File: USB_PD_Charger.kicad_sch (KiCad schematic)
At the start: 50 parts, among them J9 Conn_01x05, Q1 AOSP21321, Q2 BSH105,215, Q3 BSH105,215, Q4 BSH105,215, U1 LM3489QMM/NOPB, U2 TPS65987DDHRSHR, U3 MX25L8006EM1I-12G

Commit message: Updated schematics
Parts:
- added R30, R31: 1k, Resistor_SMD:R_0402_1005Metric, symbol Device:R_Small
- C18: LCSC C541323 -> C1603; Part_Number CC0201JRX7R8BB221 -> CL10B221KB8NNNC
- C20, C5: LCSC C105883 -> C307331; Part_Number CC0402KRX7R8BB104 -> CL05B104KB54PNC
- C21: LCSC C59782 -> C15849; Part_Number CL10B105KO8NNNC -> CL10A105KB8NNNC
- C24, C25: footprint Capacitor_SMD:C_0603_1608Metric -> Capacitor_SMD:C_0402_1005Metric; LCSC C19702 -> C15525; Part_Number CL10A106KP8NNNC -> CL05A106MQ5NUNC
- C6, C9: LCSC C106205 -> C1523; Part_Number CC0402KRX7R9BB102 -> 0402B102K500NT
- C7: value 0.1uF -> 0.1µF; LCSC C187828 -> C307331; Part_Number GMK105BJ104KV-F -> CL05B104KB54PNC
- C8: LCSC C281751 -> C1546; Part_Number CC0402KRX7R9BB101 -> 0402CG101J500NT
- R1: LCSC C107699 -> C17514; Part_Number RC0805JR-071ML -> 0805W8F1004T5E
- R10: footprint Resistor_SMD:R_0402_1005Metric -> Resistor_SMD:R_0805_2012Metric_Pad1.20x1.40mm_HandSolder; LCSC C321660 -> C17858; Part_Number RC-02W9531FT -> 0805W8F9531T5E
- R11, R12, R13, R5: footprint Resistor_SMD:R_0402_1005Metric -> Resistor_SMD:R_0603_1608Metric; LCSC C284273 -> C25803; Part_Number ARG02FTC1003 -> 0603WAF1003T5E
- R14: footprint Resistor_SMD:R_0402_1005Metric -> Resistor_SMD:R_0805_2012Metric_Pad1.20x1.40mm_HandSolder; LCSC C310249 -> C37551; Part_Number RC-02W8871FT -> 0805W8F8871T5E
- R15: footprint Resistor_SMD:R_0402_1005Metric -> Resistor_SMD:R_0805_2012Metric_Pad1.20x1.40mm_HandSolder; LCSC C166578 -> C17611; Part_Number RTT023651FTH -> 0805W8F3651T5E
- R16: footprint Resistor_SMD:R_0402_1005Metric -> Resistor_SMD:R_0805_2012Metric_Pad1.20x1.40mm_HandSolder; LCSC C258119 -> C17520; Part_Number RC-02W222JT -> 0805W8F2201T5E
- R3: value 47.5k -> 47k; LCSC C25896 -> C25792; Part_Number 0402WGF4752TCE -> 0402WGF4702TCE
- R36, R37, R39, R40, R41, R42, R45, R46: LCSC C105870 -> C25900; Part_Number RC0402JR-074K7L -> 0402WGF4701TCE
- R4: footprint Resistor_SMD:R_0402_1005Metric -> Resistor_SMD:R_0603_1608Metric; LCSC C138008 -> C22984; Part_Number RC0402FR-0730KL -> 0603WAF3002T5E
- R47: value 10.0k -> 10k; footprint Resistor_SMD:R_0201_0603Metric -> Resistor_SMD:R_0402_1005Metric; LCSC C106225 -> C25744; Part_Number RC0201FR-0710KL -> 0402WGF1002TCE
- R52: footprint Resistor_SMD:R_0201_0603Metric -> Resistor_SMD:R_0402_1005Metric; LCSC C106224 -> C25741; Part_Number RC0201FR-07100KL -> 0402WGF1003TCE
- R6: footprint Resistor_SMD:R_0402_1005Metric -> Resistor_SMD:R_0603_1608Metric; LCSC C162886 -> C22966; Part_Number RM04JTN271 -> 0603WAF2700T5E
- R9: footprint Resistor_SMD:R_0402_1005Metric -> Resistor_SMD:R_0603_1608Metric; LCSC C138063 -> C25950; Part_Number RC0402FR-0711KL -> 0603WAF1102T5E
- U2: LCSC (none) -> C2868843; Part_Number (none) -> TPS65987DDHRSHR
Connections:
- net at C6.2, U1.5 (ADJ): now also R30.2, R31.2; no longer R3.2
- new net: R3.2, R30.1, R31.1

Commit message: Updated board layout
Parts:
- U3: footprint MX25L8006EM1I-12G:SOIC127P600X175-8N -> MX25L8006EM1I-12G:MX25L8006EM1I-12G
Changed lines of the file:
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@@
 			)
 		)
-		(property "Footprint" "MX25L8006EM1I-12G:SOIC127P600X175-8N"
+		(property "Footprint" "MX25L8006EM1I-12G:MX25L8006EM1I-12G"
 			(at 214.63 128.27 0)
 			(effects

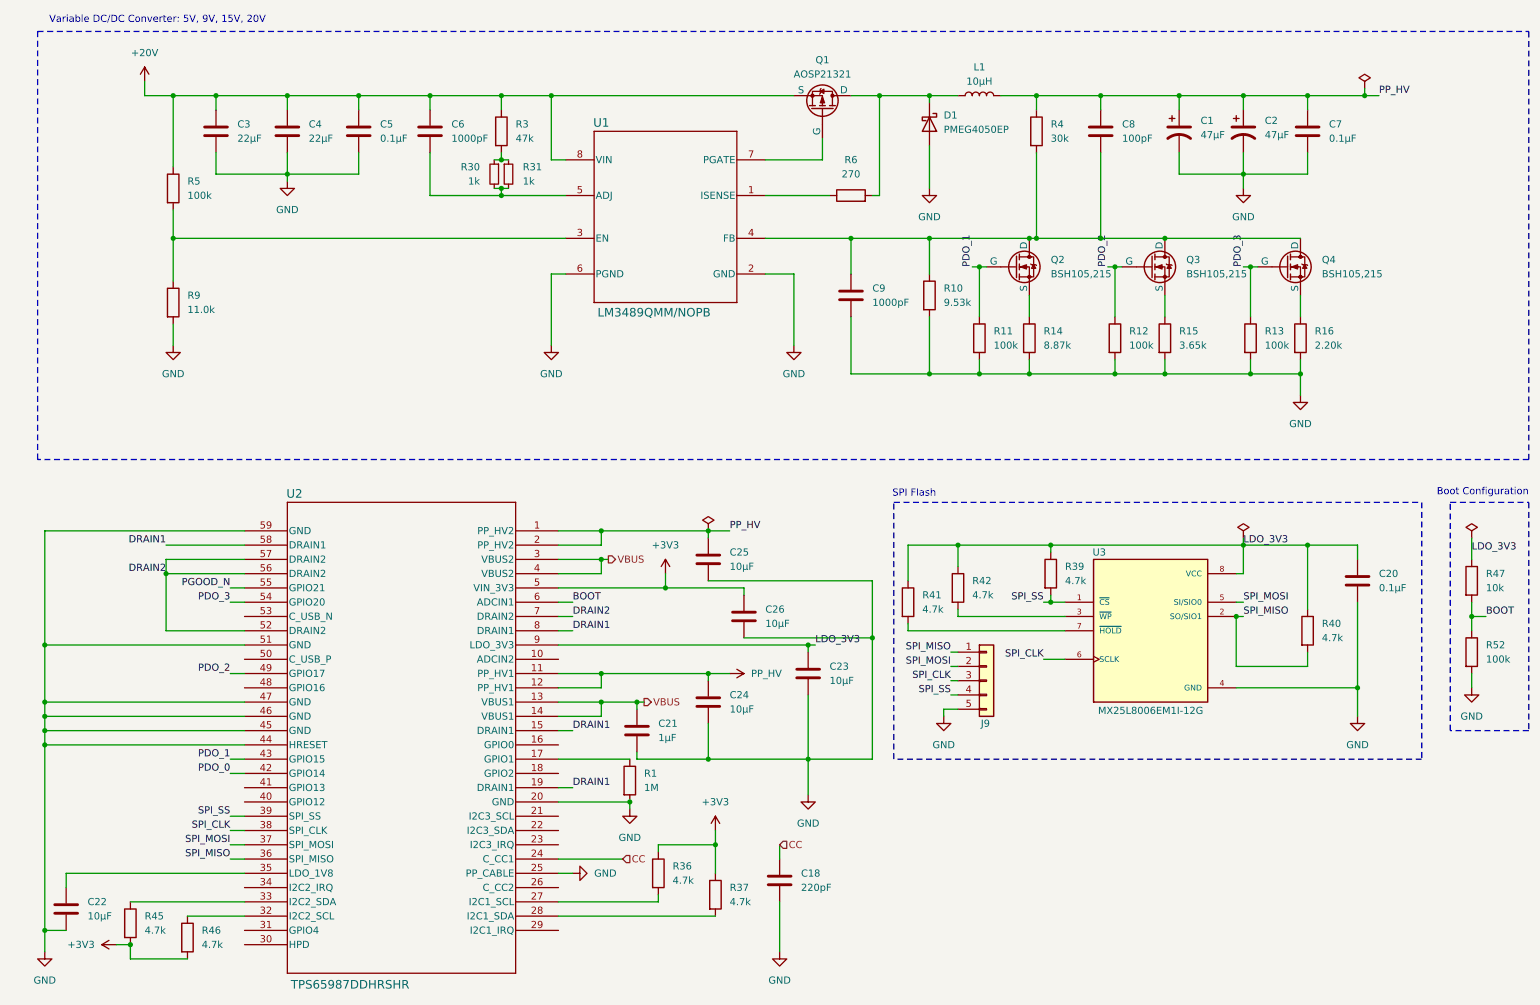
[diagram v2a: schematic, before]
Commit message: Add TPS65987D charger circuit
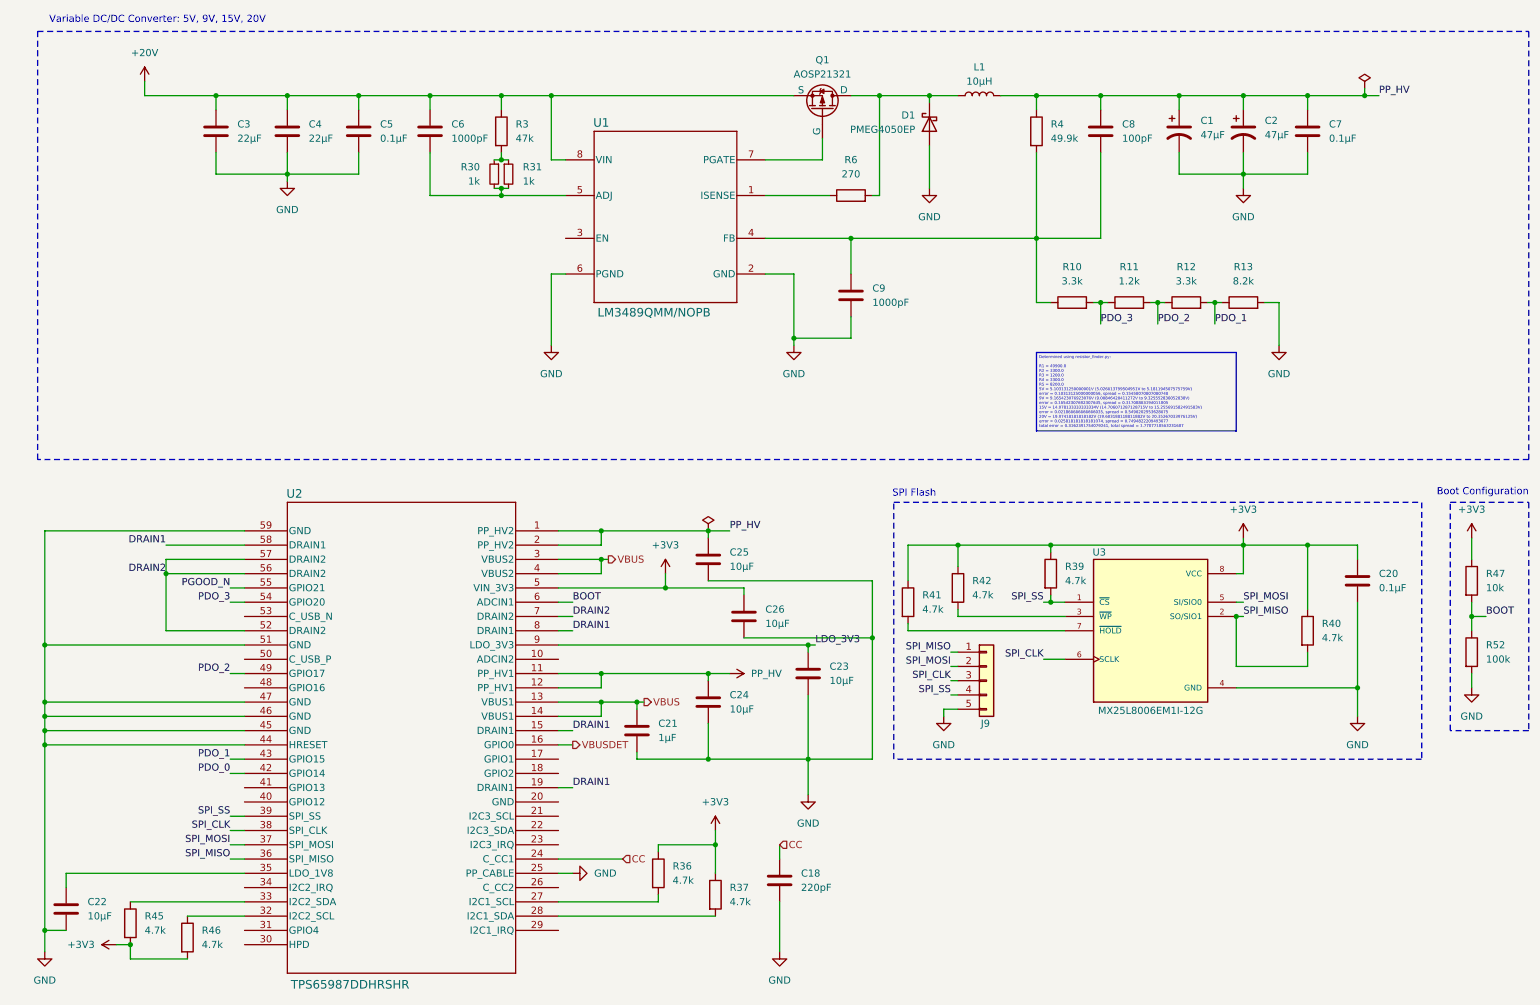
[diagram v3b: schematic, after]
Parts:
- removed Q2, Q3, Q4: BSH105,215, Package_TO_SOT_SMD:SOT-23, symbol Simulation_SPICE:NMOS
- removed R1: 1M, Resistor_SMD:R_0805_2012Metric, symbol Device:R
- removed R14: 8.87k, Resistor_SMD:R_0805_2012Metric_Pad1.20x1.40mm_HandSolder, symbol Device:R
- removed R15: 3.65k, Resistor_SMD:R_0805_2012Metric_Pad1.20x1.40mm_HandSolder, symbol Device:R
- removed R16: 2.20k, Resistor_SMD:R_0805_2012Metric_Pad1.20x1.40mm_HandSolder, symbol Device:R
- removed R5: 100k, Resistor_SMD:R_0603_1608Metric, symbol Device:R
- removed R9: 11.0k, Resistor_SMD:R_0603_1608Metric, symbol Device:R
- C18: footprint Capacitor_SMD:C_0201_0603Metric -> Capacitor_SMD:C_0402_1005Metric; LCSC C1603 -> C1530; Part_Number CL10B221KB8NNNC -> 0402B221K500NT
- R10: value 9.53k -> 3.3k; footprint Resistor_SMD:R_0805_2012Metric_Pad1.20x1.40mm_HandSolder -> Resistor_SMD:R_0402_1005Metric; LCSC C17858 -> C25890; Part_Number 0805W8F9531T5E -> 0402WGF3301TCE
- R11: value 100k -> 1.2k; footprint Resistor_SMD:R_0603_1608Metric -> Resistor_SMD:R_0402_1005Metric; LCSC C25803 -> C25862; Part_Number 0603WAF1003T5E -> 0402WGF1201TCE
- R12: value 100k -> 3.3k; footprint Resistor_SMD:R_0603_1608Metric -> Resistor_SMD:R_0402_1005Metric; LCSC C25803 -> C25890; Part_Number 0603WAF1003T5E -> 0402WGF3301TCE
- R13: value 100k -> 8.2k; footprint Resistor_SMD:R_0603_1608Metric -> Resistor_SMD:R_0402_1005Metric; LCSC C25803 -> C25924; Part_Number 0603WAF1003T5E -> 0402WGF8201TCE
- R4: value 30k -> 49.9k; footprint Resistor_SMD:R_0603_1608Metric -> Resistor_SMD:R_0402_1005Metric; LCSC C22984 -> C25897; Part_Number 0603WAF3002T5E -> 0402WGF4992TCE
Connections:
- net +3V3: now also C20.1, R39.1, R40.1, R41.1, R42.1, R47.1, U3.8 (VCC)
- net GND: no longer R10.2, R11.2, R12.2, U2.20 (GND)
- net LDO_3V3: no longer C20.1, R39.1, R40.1, R41.1, R42.1, R47.1, U3.8 (VCC)
- net PDO_1: now also R12.2, R13.1; no longer R11.1
- net PDO_2: now also R11.2
- net PDO_3: now also R10.2, R11.1; no longer R13.1
- net VBUSDET: now reaches U2.16 (GPIO0)
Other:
- moved on the sheet: D1

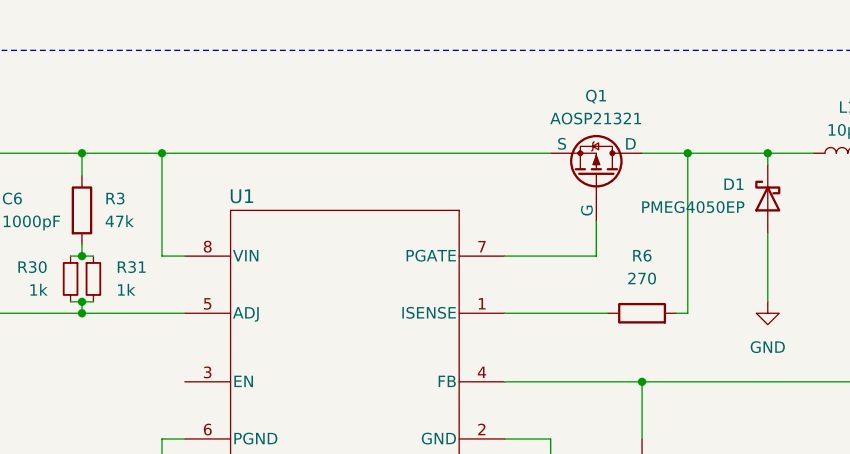
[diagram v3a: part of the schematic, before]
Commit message: Replace AOSP21321 with AON7403 and update 3D models
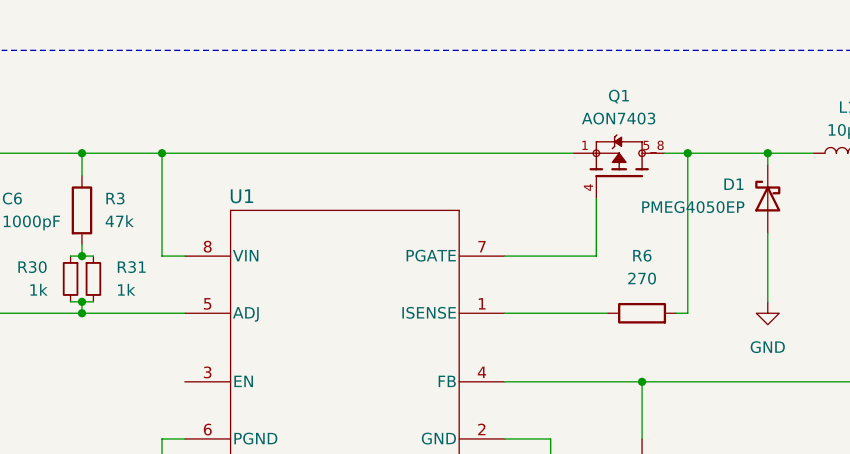
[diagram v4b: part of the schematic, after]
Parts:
- removed Q1: AOSP21321, AOSP21321:AOSP21321, symbol Simulation_SPICE:PMOS
- added Q1: AON7403, AON7403:TRANS_AON7403, symbol AON7403:AON7403
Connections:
- net +20V: now also Q1.1
- net at D1.1 (K), L1.1, R6.2: now also Q1.5_8
- net at U1.7 (PGATE): now also Q1.4
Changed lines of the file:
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@@
 	)
 	(junction
+		(at 166.37 33.02)
+		(diameter 0)
+		(color 0 0 0 0)
+	)
+	(junction
 		(at 153.67 151.13)
 		(diameter 0)
@@
 	)
 	(junction
-		(at 166.37 33.02)
-		(diameter 0)
-		(color 0 0 0 0)
-	)
-	(junction
 		(at 153.67 130.81)
 		(diameter 0)
@@
 	(wire
 		(pts
-			(xy 107.95 33.02) (xy 151.13 33.02)
+			(xy 107.95 33.02) (xy 153.67 33.02)
 		)
 		(stroke
@@
 	(wire
 		(pts
+			(xy 156.21 38.1) (xy 156.21 44.45)
+		)
+		(stroke
+			(width 0)
+			(type default)
+		)
+	)
+	(wire
+		(pts
 			(xy 39.37 118.11) (xy 39.37 128.27)
 		)
@@
 	(wire
 		(pts
+			(xy 163.83 33.02) (xy 166.37 33.02)
+		)
+		(stroke
+			(width 0)
+			(type default)
+		)
+	)
+	(wire
+		(pts
 			(xy 180.34 113.03) (xy 196.85 113.03)
 		)
@@
 	(wire
 		(pts
-			(xy 156.21 44.45) (xy 156.21 40.64)
-		)
-		(stroke
-			(width 0)
-			(type default)
-		)
-	)
-	(wire
-		(pts
 			(xy 86.36 33.02) (xy 86.36 35.56)
 		)
@@
 	(wire
 		(pts
-			(xy 161.29 33.02) (xy 166.37 33.02)
-		)
-		(stroke
-			(width 0)
-			(type default)
-		)
-	)
-	(wire
-		(pts
 			(xy 109.22 156.21) (xy 111.76 156.21)
 		)
@@
 	)
 	(symbol
-		(lib_id "Simulation_SPICE:PMOS")
-		(at 156.21 35.56 270)
-		(mirror x)
+		(lib_id "power:GND")
+		(at 177.8 143.51 0)
 		(unit 1)
 		(exclude_from_sim no)
@@
 		(dnp no)
 		(fields_autoplaced yes)
-		(property "Reference" "Q1"
-			(at 156.21 26.67 90)
-			(effects
-				(font
-					(size 1.27 1.27)
-				)
-			)
-		)
-		(property "Value" "AOSP21321"
-			(at 156.21 29.21 90)
-			(effects
-				(font
-					(size 1.27 1.27)
-				)
-			)
-		)
-		(property "Footprint" "AOSP21321:AOSP21321"
-			(at 158.75 30.48 0)
-			(effects
-				(font
-					(size 1.27 1.27)
-				)
-				(hide yes)
-			)
-		)
-		(property "Datasheet" "https://ngspice.sourceforge.io/docs/ngspice-html-manual/manual.xhtml#cha_MOSFETs"
-			(at 143.51 35.56 0)
+		(property "Reference" "#PWR027"
+			(at 177.8 149.86 0)
 			(effects
 				(font
@@
 			)
 		)
-		(property "Description" "P-MOSFET transistor, drain/source/gate"
-			(at 156.21 35.56 0)
+		(property "Value" "GND"
+			(at 177.8 148.59 0)
 			(effects
 				(font
 					(size 1.27 1.27)
 				)
-				(hide yes)
 			)
 		)
-		(property "Sim.Device" "PMOS"
-			(at 139.065 35.56 0)
+		(property "Footprint" ""
+			(at 177.8 143.51 0)
 			(effects
 				(font
@@
 			)
 		)
-		(property "Sim.Type" "VDMOS"
-			(at 137.16 35.56 0)
+		(property "Datasheet" ""
+			(at 177.8 143.51 0)
 			(effects
 				(font
@@
 			)
 		)
-		(property "Sim.Pins" "1=D 2=G 3=S"
-			(at 140.97 35.56 0)
+		(property "Description" "Power symbol creates a global label with name \"GND\" , ground"
+			(at 177.8 143.51 0)
 			(effects
 				(font
@@
 			)
 		)
-		(property "Part_Number" "AON7403"
-			(at 156.21 35.56 90)
-			(effects
-				(font
-					(size 1.27 1.27)
-				)
-				(hide yes)
-			)
+		(pin "1"
 		)
-		(property "LCSC" "C560863"
-			(at 156.21 35.56 90)
-			(effects
-				(font
-					(size 1.27 1.27)
+		(instances
+			(project "XG_Mobile_Dock"
+				(path "/f97e6956-ab08-42cb-8fed-03fa58e87f0e/fa35204a-fbf7-48de-bc5b-11fc2e29f675"
+					(reference "#PWR027")
+					(unit 1)
 				)
-				(hide yes)
 			)
 		)
-		(property "Vend" ""
-			(at 156.21 35.56 0)
+	)
+	(symbol
+		(lib_id "AON7403:AON7403")
+		(at 158.75 35.56 90)
+		(unit 1)
+		(exclude_from_sim no)
+		(in_bom yes)
+		(on_board yes)
+		(dnp no)
+		(fields_autoplaced yes)
+		(property "Reference" "Q1"
+			(at 158.75 26.67 90)
 			(effects
 				(font
 					(size 1.27 1.27)
 				)
-				(hide yes)
 			)
 		)
-		(property "Vendor" ""
-			(at 156.21 35.56 0)
+		(property "Value" "AON7403"
+			(at 158.75 29.21 90)
 			(effects
 				(font
 					(size 1.27 1.27)
 				)
-				(hide yes)
 			)
 		)
-		(property "Category" ""
-			(at 156.21 35.56 0)
+		(property "Footprint" "AON7403:TRANS_AON7403"
+			(at 158.75 35.56 0)
 			(effects
 				(font
 					(size 1.27 1.27)
 				)
+				(justify bottom)
 				(hide yes)
 			)
 		)
-		(property "DK_Datasheet_Link" ""
-			(at 156.21 35.56 0)
+		(property "Datasheet" ""
+			(at 158.75 35.56 0)
 			(effects
 				(font
@@
 			)
 		)
-		(property "DK_Detail_Page" ""
-			(at 156.21 35.56 0)
+		(property "Description" ""
+			(at 158.75 35.56 0)
 			(effects
 				(font
@@
 			)
 		)
-		(property "Family" ""
-			(at 156.21 35.56 0)
+		(property "PARTREV" "G"
+			(at 158.75 35.56 0)
 			(effects
 				(font
 					(size 1.27 1.27)
 				)
+				(justify bottom)
 				(hide yes)
 			)
 		)
-		(property "MPN" ""
-			(at 156.21 35.56 0)
+		(property "STANDARD" "Manufacturer Recommendations"
+			(at 158.75 35.56 0)
 			(effects
 				(font
 					(size 1.27 1.27)
 				)
+				(justify bottom)
 				(hide yes)
 			)
 		)
-		(property "Manufacturer" ""
-			(at 156.21 35.56 0)
+		(property "MAXIMUM_PACKAGE_HEIGHT" "0.9 mm"
+			(at 158.75 35.56 0)
 			(effects
 				(font
 					(size 1.27 1.27)
 				)
+				(justify bottom)
 				(hide yes)
 			)
 		)
-		(property "Status" ""
-			(at 156.21 35.56 0)
+		(property "MANUFACTURER" "Alpha & Omega"
+			(at 158.75 35.56 0)
 			(effects
 				(font
 					(size 1.27 1.27)
 				)
+				(justify bottom)
 				(hide yes)
 			)
 		)
-		(pin "1"
-		)
-		(pin "2"
-		)
-		(pin "3"
-		)
-		(instances
-			(project "XG_Mobile_Dock"
-				(path "/f97e6956-ab08-42cb-8fed-03fa58e87f0e/fa35204a-fbf7-48de-bc5b-11fc2e29f675"
-					(reference "Q1")
-					(unit 1)
-				)
-			)
-		)
-	)
-	(symbol
-		(lib_id "power:GND")
-		(at 177.8 143.51 0)
-		(unit 1)
-		(exclude_from_sim no)
-		(in_bom yes)
-		(on_board yes)
-		(dnp no)
-		(fields_autoplaced yes)
-		(property "Reference" "#PWR027"
-			(at 177.8 149.86 0)
+		(property "Part_Number" "AON7403"
+			(at 158.75 35.56 90)
 			(effects
 				(font
@@
 			)
 		)
-		(property "Value" "GND"
-			(at 177.8 148.59 0)
-			(effects
-				(font
-					(size 1.27 1.27)
-				)
-			)
-		)
-		(property "Footprint" ""
-			(at 177.8 143.51 0)
+		(property "LCSC" "C115841"
+			(at 158.75 35.56 90)
 			(effects
 				(font
@@
 			)
 		)
-		(property "Datasheet" ""
-			(at 177.8 143.51 0)
-			(effects
-				(font
-					(size 1.27 1.27)
-				)
-				(hide yes)
-			)
+		(pin "5_8"
 		)
-		(property "Description" "Power symbol creates a global label with name \"GND\" , ground"
-			(at 177.8 143.51 0)
-			(effects
-				(font
-					(size 1.27 1.27)
-				)
-				(hide yes)
-			)
+		(pin "4"
 		)
 		(pin "1"
@@
 			(project "XG_Mobile_Dock"
 				(path "/f97e6956-ab08-42cb-8fed-03fa58e87f0e/fa35204a-fbf7-48de-bc5b-11fc2e29f675"
-					(reference "#PWR027")
+					(reference "Q1")
 					(unit 1)
 				)

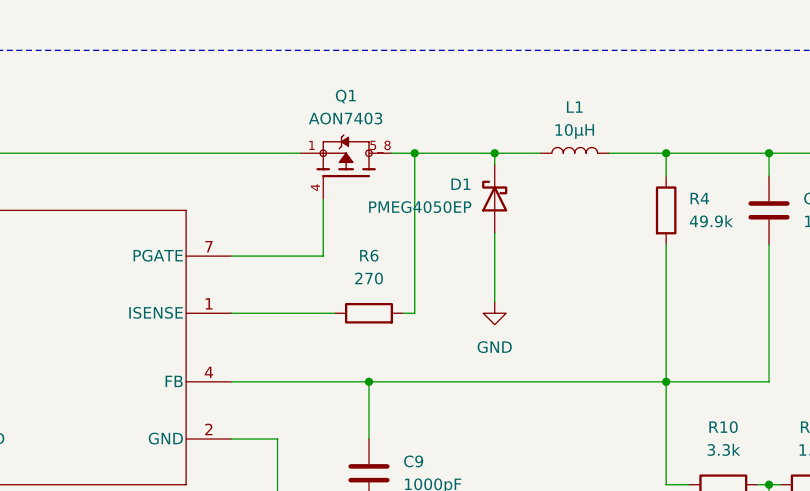
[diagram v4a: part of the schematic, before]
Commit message: new power blocks
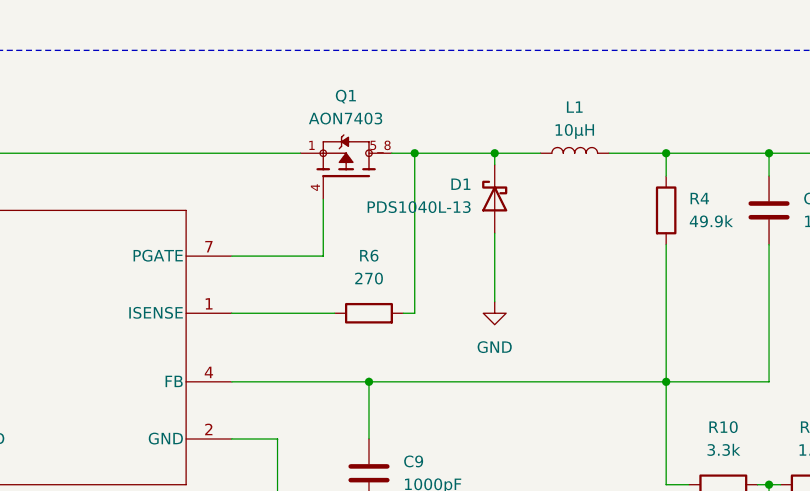
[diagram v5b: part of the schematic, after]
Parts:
- D1: value PMEG4050EP -> PDS1040L-13; footprint Diode_SMD:D_SOD-128 -> Diode_SMD:D_PowerDI-5; LCSC C96235 -> C154714; Part_Number PMEG4050EP,115 -> PDS1040L-13
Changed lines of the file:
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@@
 			)
 		)
-		(property "Value" "PMEG4050EP"
+		(property "Value" "PDS1040L-13"
 			(at 172.72 39.0524 90)
 			(effects
@@
 			)
 		)
-		(property "Footprint" "Diode_SMD:D_SOD-128"
+		(property "Footprint" "Diode_SMD:D_PowerDI-5"
 			(at 179.705 38.1 0)
 			(effects
@@
 			)
 		)
-		(property "Description" "40V, 5A low Vf Schottky barrier rectifier, SOD-128"
+		(property "Description" "40V, 10A Schottky barrier rectifier"
 			(at 175.26 38.1 0)
 			(effects
@@
 			)
 		)
-		(property "Part_Number" "PMEG4050EP,115"
+		(property "Part_Number" "PDS1040L-13"
 			(at 175.26 38.1 90)
 			(effects
@@
 			)
 		)
-		(property "LCSC" "C96235"
+		(property "LCSC" "C154714"
 			(at 175.26 38.1 90)
 			(effects
